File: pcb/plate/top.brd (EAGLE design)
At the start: 109 x 96 mm, 27 parts

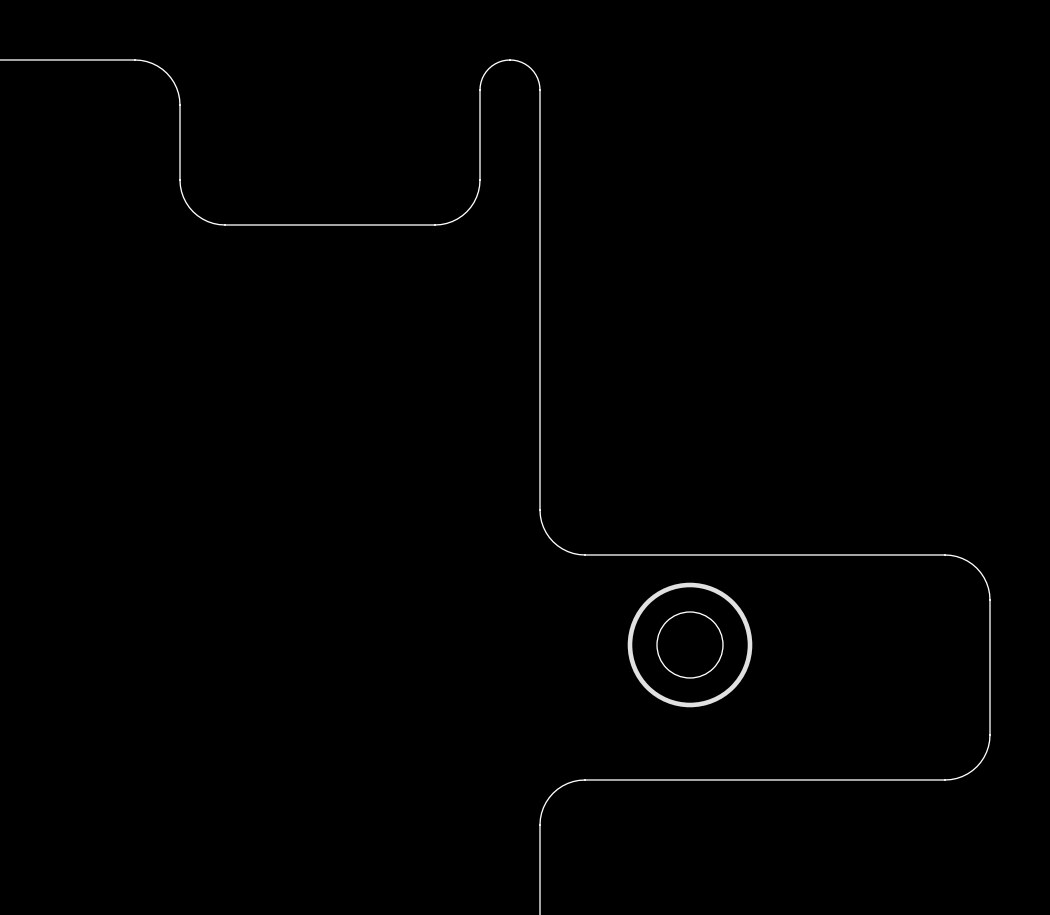
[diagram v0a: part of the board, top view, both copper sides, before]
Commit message: adjusted top plate cutout, removed unused screw hole
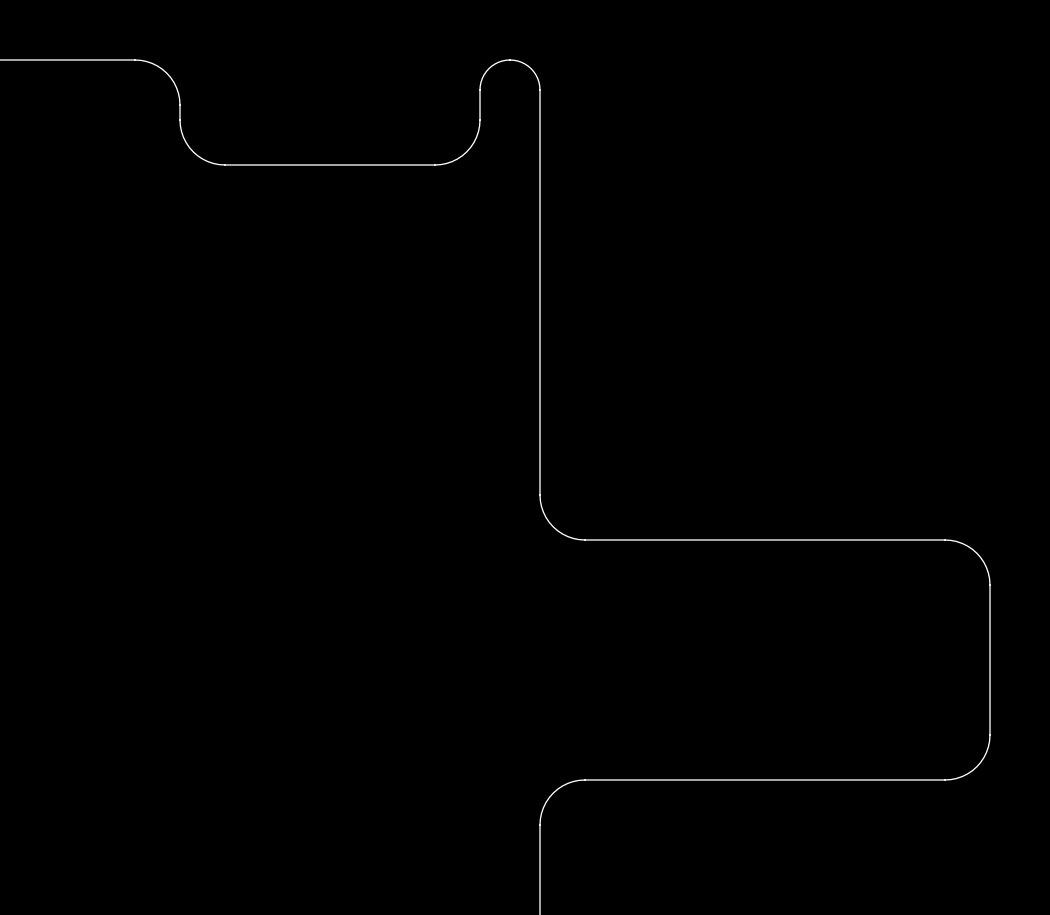
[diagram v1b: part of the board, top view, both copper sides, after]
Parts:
- removed U$17: M2_SCREW_DEV, duckypad:M2_SCREW_FOOT
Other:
- outline, holes or cut-outs redrawn
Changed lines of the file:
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@@
 <wire x1="3.5" y1="96" x2="80.5" y2="96" width="0" layer="20"/>
 <wire x1="80.5" y1="96" x2="82" y2="94.5" width="0" layer="20" curve="-90"/>
-<wire x1="82" y1="94.5" x2="82" y2="92" width="0" layer="20"/>
-<wire x1="82" y1="92" x2="83.5" y2="90.5" width="0" layer="20" curve="90"/>
-<wire x1="83.5" y1="90.5" x2="90.5" y2="90.5" width="0" layer="20"/>
-<wire x1="90.5" y1="90.5" x2="92" y2="92" width="0" layer="20" curve="90"/>
-<wire x1="92" y1="92" x2="92" y2="95" width="0" layer="20"/>
+<wire x1="82" y1="94.5" x2="82" y2="94" width="0" layer="20"/>
+<wire x1="82" y1="94" x2="83.5" y2="92.5" width="0" layer="20" curve="90"/>
+<wire x1="83.5" y1="92.5" x2="90.5" y2="92.5" width="0" layer="20"/>
+<wire x1="90.5" y1="92.5" x2="92" y2="94" width="0" layer="20" curve="90"/>
+<wire x1="92" y1="94" x2="92" y2="95" width="0" layer="20"/>
 <wire x1="72.5" y1="0" x2="3.5" y2="0" width="0" layer="20"/>
 <wire x1="3.5" y1="0" x2="0" y2="3.5" width="0" layer="20" curve="-90"/>
@@
 <wire x1="76" y1="53" x2="76" y2="3.5" width="0" layer="20"/>
 <wire x1="76" y1="3.5" x2="72.5" y2="0" width="0" layer="20" curve="-90"/>
-<wire x1="95.5" y1="79.5" x2="107.5" y2="79.5" width="0" layer="20"/>
-<wire x1="107.5" y1="79.5" x2="109" y2="78" width="0" layer="20" curve="-90"/>
-<wire x1="109" y1="78" x2="109" y2="73.5" width="0" layer="20"/>
+<wire x1="94" y1="95" x2="94" y2="81.5" width="0" layer="20"/>
+<wire x1="94" y1="81.5" x2="95.5" y2="80" width="0" layer="20" curve="90"/>
+<wire x1="95.5" y1="80" x2="107.5" y2="80" width="0" layer="20"/>
+<wire x1="107.5" y1="80" x2="109" y2="78.5" width="0" layer="20" curve="-90"/>
+<wire x1="109" y1="78.5" x2="109" y2="73.5" width="0" layer="20"/>
 <wire x1="109" y1="73.5" x2="107.5" y2="72" width="0" layer="20" curve="-90"/>
 <wire x1="107.5" y1="72" x2="95.5" y2="72" width="0" layer="20"/>
@@
 <wire x1="92" y1="95" x2="93" y2="96" width="0" layer="20" curve="-90"/>
 <wire x1="93" y1="96" x2="94" y2="95" width="0" layer="20" curve="-90"/>
-<wire x1="94" y1="95" x2="94" y2="81" width="0" layer="20"/>
-<wire x1="94" y1="81" x2="95.5" y2="79.5" width="0" layer="20" curve="90"/>
 <text x="92" y="44" size="1.778" layer="51">big round corner 3.5mm</text>
 </plain>
@@
 <element name="U$12" library="duckypad" package="M2_SCREW_FOOT" value="M2_SCREW_DEV" x="38.5" y="38.5" smashed="yes"/>
 <element name="U$13" library="duckypad" package="M2_SCREW_FOOT" value="M2_SCREW_DEV" x="57.5" y="19.5" smashed="yes"/>
-<element name="U$17" library="duckypad" package="M2_SCREW_FOOT" value="M2_SCREW_DEV" x="99" y="76.5" smashed="yes"/>
 <element name="U$14" library="duckypad" package="M2_SCREW_FOOT" value="M2_SCREW_DEV" x="19.5" y="76.5" smashed="yes"/>
 <element name="U$22" library="duckypad" package="M2_SCREW_FOOT" value="M2_SCREW_DEV" x="19.5" y="19.5" smashed="yes"/>
